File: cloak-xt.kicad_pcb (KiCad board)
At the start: 2 copper layers, 20.3 x 50.8 mm, 23 parts, among them J1 USB_C_Receptacle_USB2.0, J2 Conn_01x20, J3 Conn_01x20, U1 STM32F072CBT6, U2 PRTR5V0U2X, U3 XC6206PxxxMR-Regulator_Linear

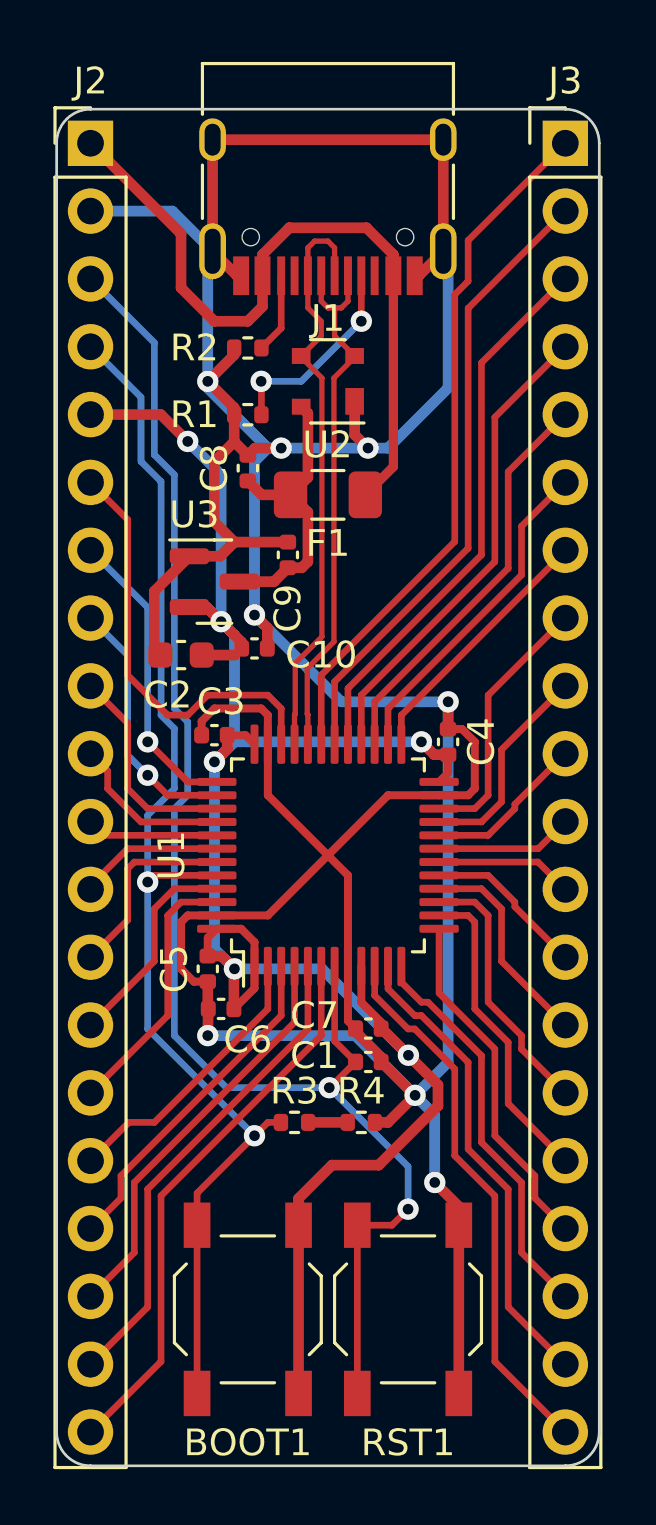
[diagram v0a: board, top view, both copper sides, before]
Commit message: Remove pin headers and edge cuts
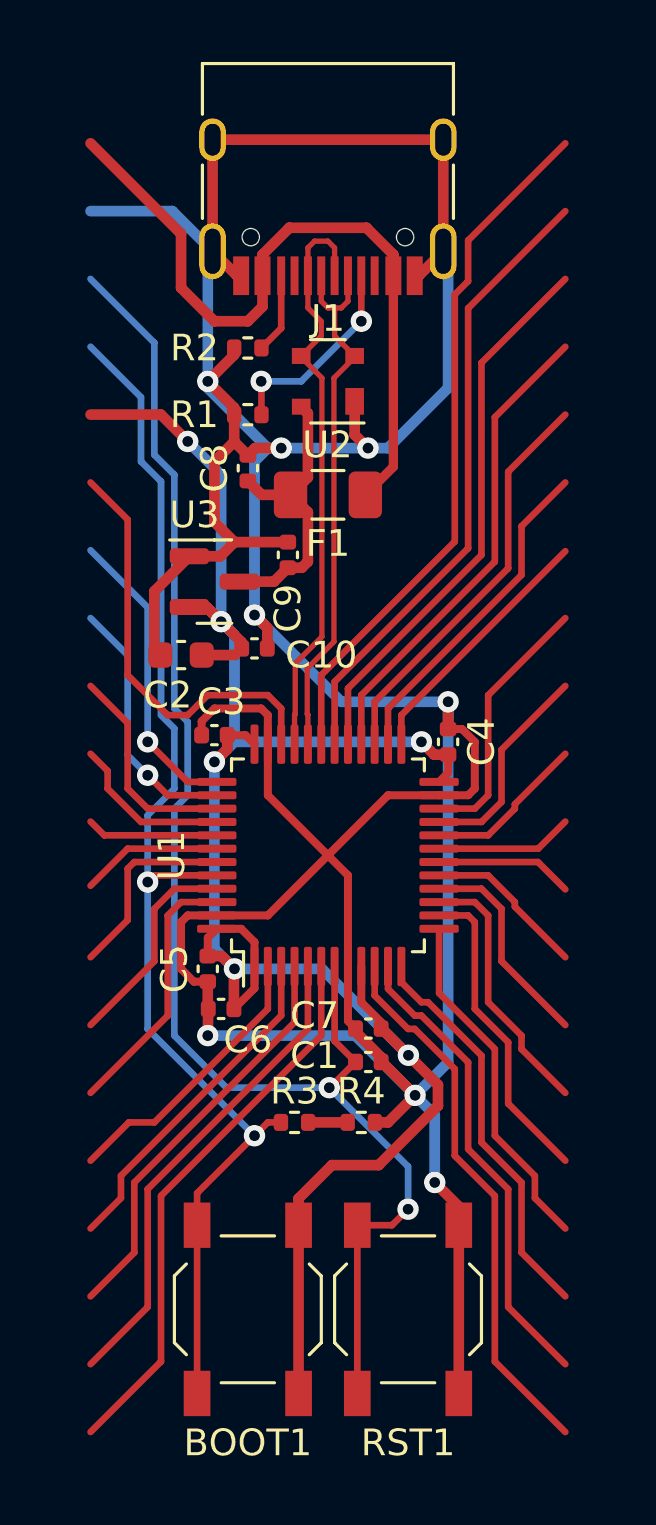
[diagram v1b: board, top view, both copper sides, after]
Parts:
- removed J2, J3: Conn_01x20, Connector_PinHeader_2.54mm:PinHeader_1x20_P2.54mm_Vertical
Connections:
- U2 pad 2: D_N -> D-
- U2 pad 3: D_P -> D+
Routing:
- net D_P: track 22.1 -> 0.00 mm
- net D+: track 0.00 -> 22.1 mm
- net D_N: track 20.5 -> 0.00 mm
- net D-: track 0.00 -> 20.5 mm
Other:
- board outline removed
